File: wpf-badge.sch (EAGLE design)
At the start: 6 parts, among them SW1 1825910-6

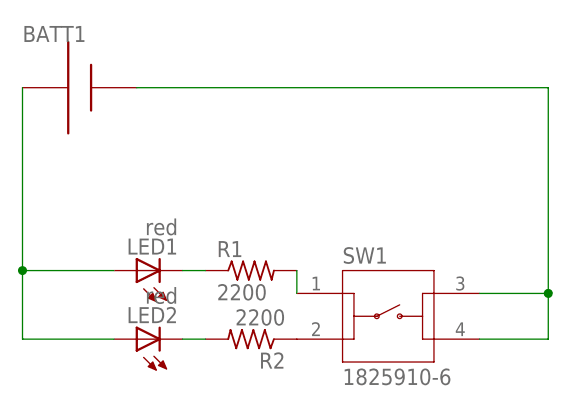
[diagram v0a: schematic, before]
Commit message: Tweak more board positioning. Minor update to schematic.
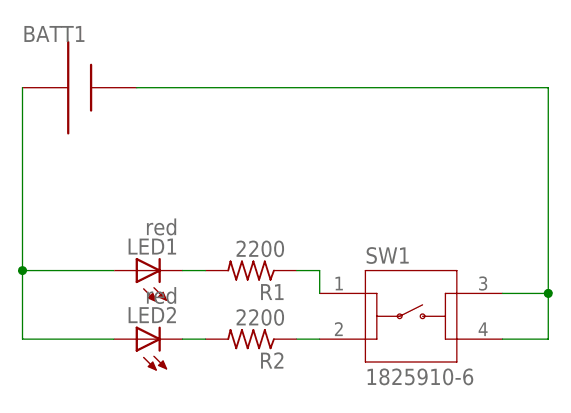
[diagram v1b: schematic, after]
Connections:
- net N$2: now also R1.2; no longer R1.1
- net N$4: now also R1.1; no longer R1.2
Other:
- moved on the sheet: R1, SW1
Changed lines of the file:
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@@
 </variantdefs>
 <classes>
-<class number="0" name="default" width="1" drill="1">
-<clearance class="0" value="0.8"/>
+<class number="0" name="default" width="0.508" drill="0.508">
+<clearance class="0" value="0.508"/>
 </class>
 </classes>
@@
 <attribute name="VALUE" x="42.672" y="41.275" size="1.778" layer="96" rot="R180"/>
 </instance>
-<instance part="R1" gate="G$1" x="50.8" y="35.56" smashed="yes">
-<attribute name="NAME" x="46.99" y="37.0586" size="1.778" layer="95"/>
-<attribute name="VALUE" x="46.99" y="32.258" size="1.778" layer="96"/>
+<instance part="R1" gate="G$1" x="50.8" y="35.56" smashed="yes" rot="R180">
+<attribute name="NAME" x="54.61" y="34.0614" size="1.778" layer="95" rot="R180"/>
+<attribute name="VALUE" x="54.61" y="38.862" size="1.778" layer="96" rot="R180"/>
 </instance>
 <instance part="R2" gate="G$1" x="50.8" y="27.94" smashed="yes" rot="R180">
@@
 <attribute name="VALUE" x="42.672" y="33.655" size="1.778" layer="96" rot="R180"/>
 </instance>
-<instance part="SW1" gate="G$1" x="66.04" y="30.48" smashed="yes">
-<attribute name="NAME" x="60.9503" y="36.33315" size="1.803440625" layer="95"/>
-<attribute name="VALUE" x="60.951690625" y="22.84753125" size="1.802940625" layer="96"/>
+<instance part="SW1" gate="G$1" x="68.58" y="30.48" smashed="yes">
+<attribute name="NAME" x="63.4903" y="36.33315" size="1.803440625" layer="95"/>
+<attribute name="VALUE" x="63.491690625" y="22.84753125" size="1.802940625" layer="96"/>
 </instance>
 </instances>
@@
 </busses>
 <nets>
-<net name="N$2" class="0">
-<segment>
-<pinref part="LED1" gate="G$1" pin="C"/>
-<pinref part="R1" gate="G$1" pin="1"/>
-<wire x1="43.18" y1="35.56" x2="45.72" y2="35.56" width="0.1524" layer="91"/>
-</segment>
-</net>
 <net name="N$3" class="0">
 <segment>
@@
 <wire x1="83.82" y1="55.88" x2="38.1" y2="55.88" width="0.1524" layer="91"/>
 <pinref part="SW1" gate="G$1" pin="3"/>
-<wire x1="76.2" y1="33.02" x2="83.82" y2="33.02" width="0.1524" layer="91"/>
+<wire x1="78.74" y1="33.02" x2="83.82" y2="33.02" width="0.1524" layer="91"/>
 <wire x1="83.82" y1="33.02" x2="83.82" y2="55.88" width="0.1524" layer="91"/>
 <pinref part="SW1" gate="G$1" pin="4"/>
-<wire x1="76.2" y1="27.94" x2="83.82" y2="27.94" width="0.1524" layer="91"/>
+<wire x1="78.74" y1="27.94" x2="83.82" y2="27.94" width="0.1524" layer="91"/>
 <wire x1="83.82" y1="27.94" x2="83.82" y2="33.02" width="0.1524" layer="91"/>
 <junction x="83.82" y="33.02"/>
@@
 </segment>
 </net>
-<net name="N$4" class="0">
-<segment>
-<pinref part="R1" gate="G$1" pin="2"/>
-<pinref part="SW1" gate="G$1" pin="1"/>
-<wire x1="55.88" y1="33.02" x2="55.88" y2="35.56" width="0.1524" layer="91"/>
-</segment>
-</net>
 <net name="N$5" class="0">
 <segment>
 <pinref part="R2" gate="G$1" pin="1"/>
 <pinref part="SW1" gate="G$1" pin="2"/>
+<wire x1="58.42" y1="27.94" x2="55.88" y2="27.94" width="0.1524" layer="91"/>
 </segment>
 </net>
@@
 </segment>
 </net>
+<net name="N$2" class="0">
+<segment>
+<pinref part="LED1" gate="G$1" pin="C"/>
+<pinref part="R1" gate="G$1" pin="2"/>
+<wire x1="43.18" y1="35.56" x2="45.72" y2="35.56" width="0.1524" layer="91"/>
+</segment>
+</net>
+<net name="N$4" class="0">
+<segment>
+<pinref part="R1" gate="G$1" pin="1"/>
+<pinref part="SW1" gate="G$1" pin="1"/>
+<wire x1="55.88" y1="35.56" x2="58.42" y2="35.56" width="0.1524" layer="91"/>
+<wire x1="58.42" y1="35.56" x2="58.42" y2="33.02" width="0.1524" layer="91"/>
+</segment>
+</net>
